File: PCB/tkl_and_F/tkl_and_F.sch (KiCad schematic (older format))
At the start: 18 parts

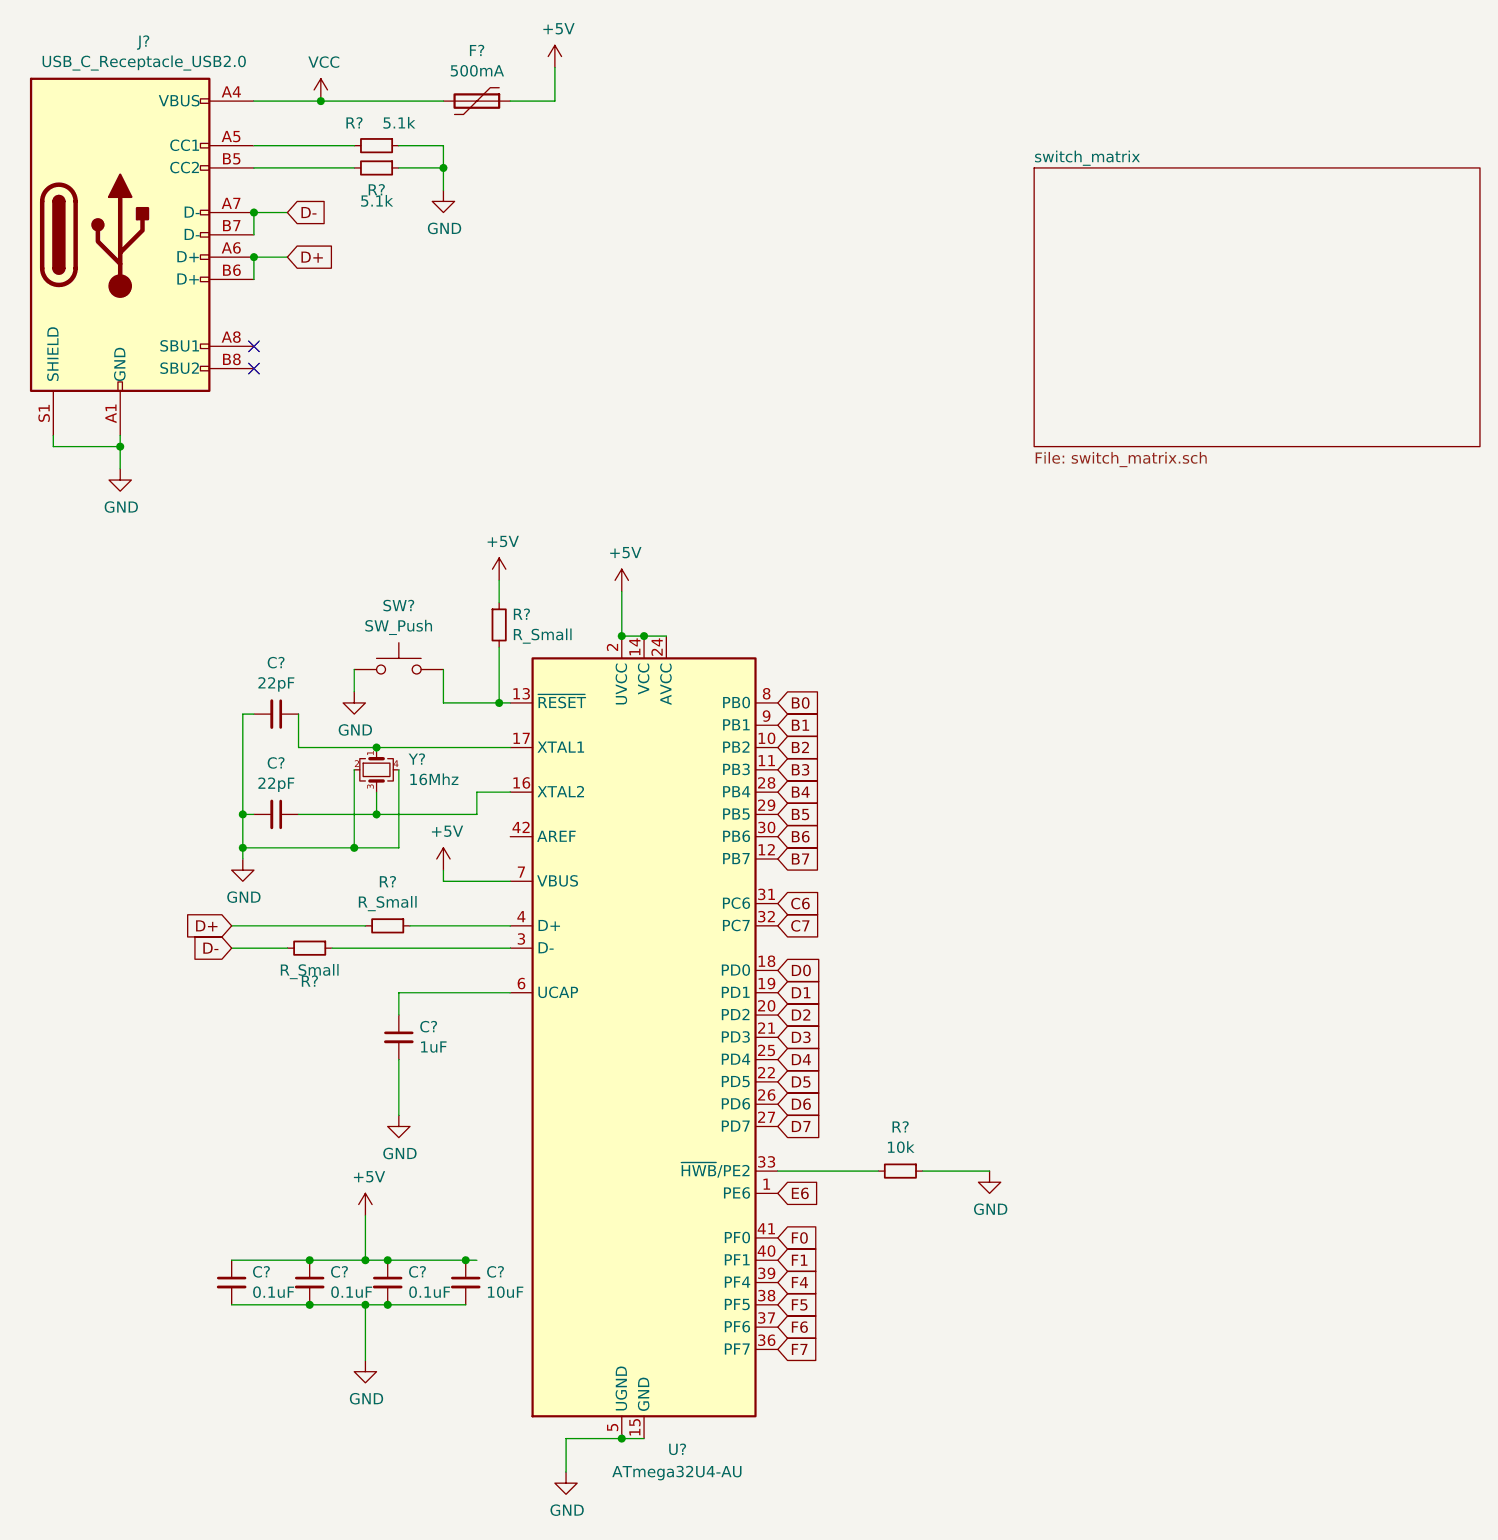
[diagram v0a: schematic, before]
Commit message: footprint assigment
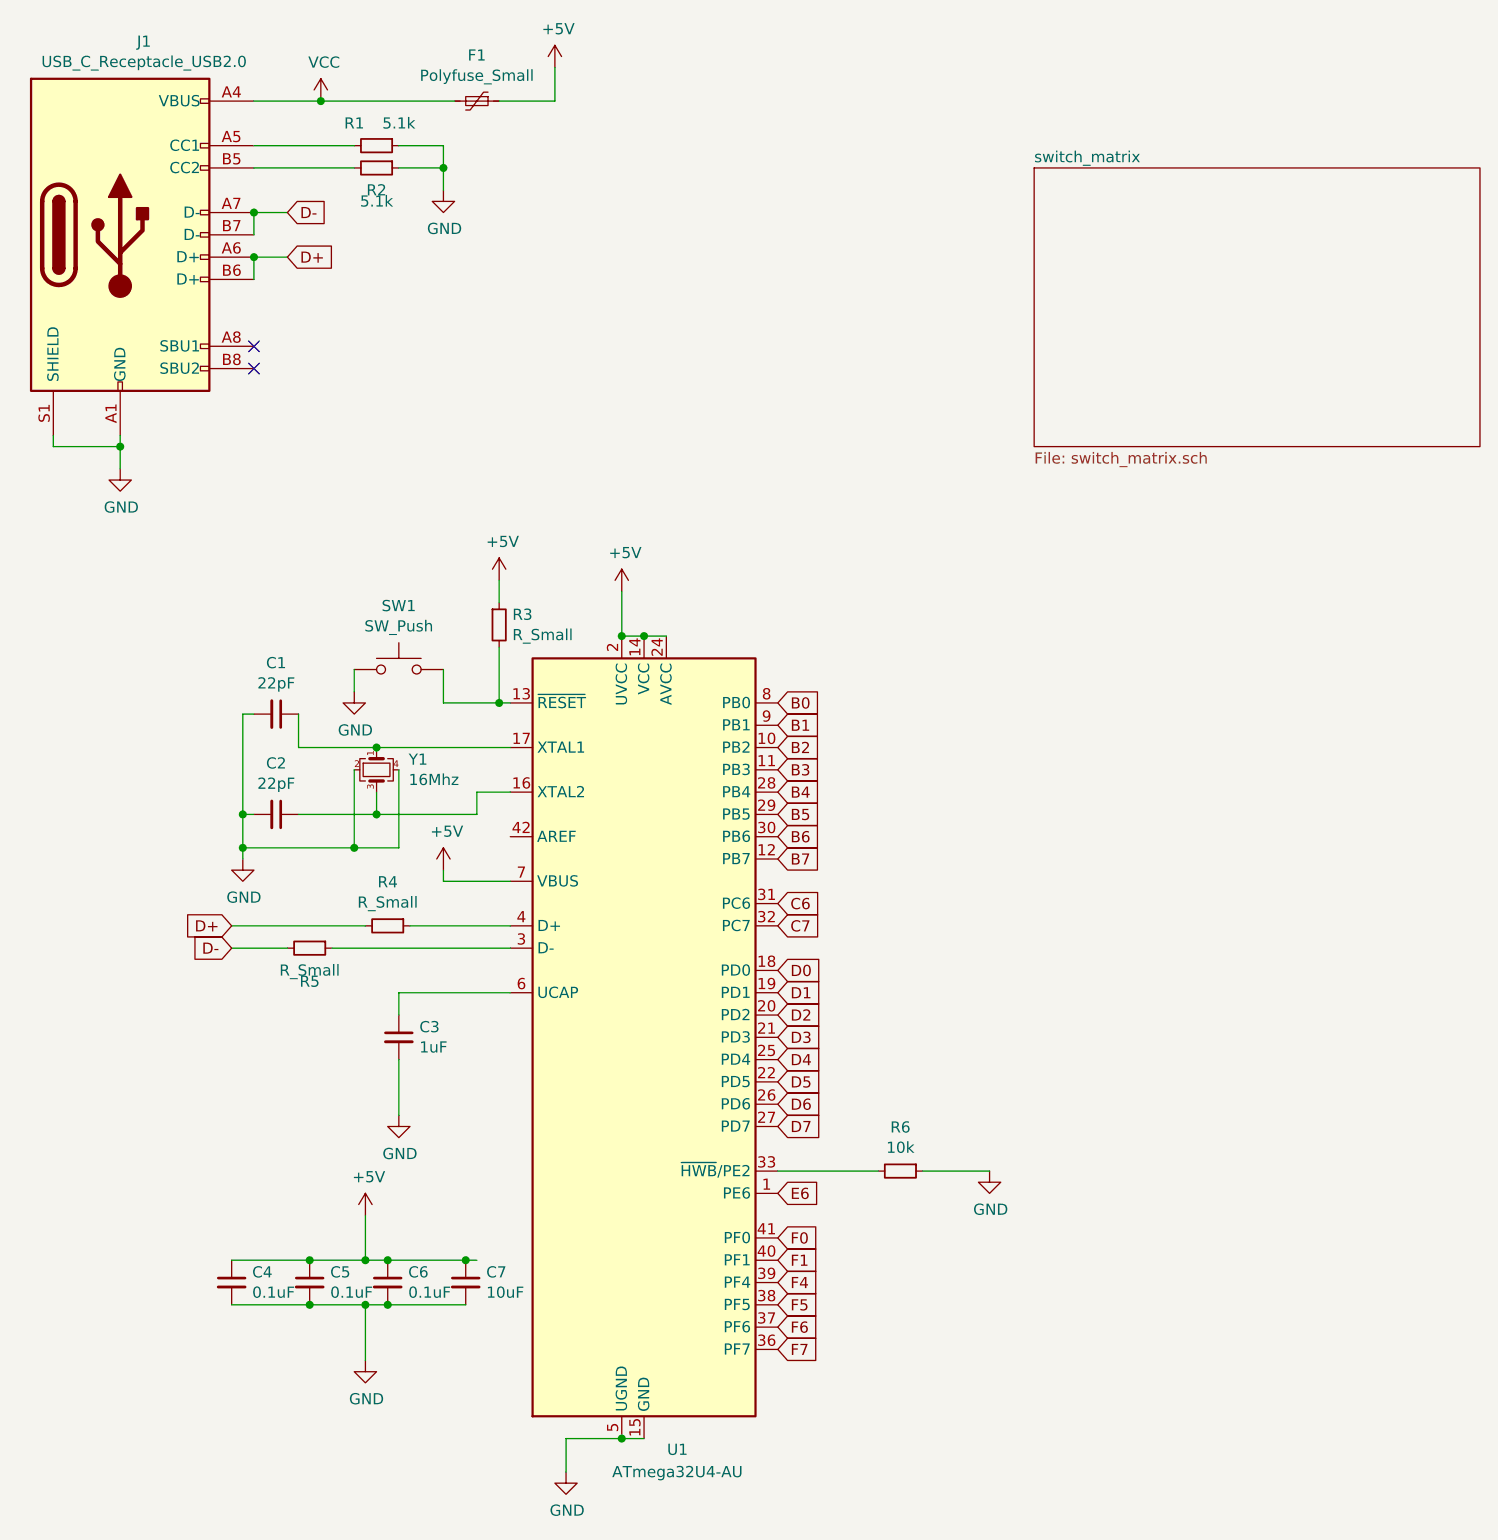
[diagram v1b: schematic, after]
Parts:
- removed F?: 500mA, symbol device:Polyfuse
- added F1: Polyfuse_Small, Fuse:Fuse_1206_3216Metric, symbol device:Polyfuse_Small
- C1, C2, C3, C4, C5, C6, C7: renamed from C?; footprint (none) -> Capacitors_SMD:C_0805
- J1: renamed from J?; footprint (none) -> Connectors_USB:USB_C_Receptacle_Amphenol_12401548E4-2A
- R1, R2, R3, R4, R5, R6: renamed from R?; footprint (none) -> Resistors_SMD:R_0805_HandSoldering
- SW1: renamed from SW?; footprint (none) -> random-keyboard-parts:SKQG-1155865
- Y1: renamed from Y?; footprint (none) -> Crystals:Crystal_SMD_3225-4pin_3.2x2.5mm_HandSoldering
- gave numbers to parts that had none: 1
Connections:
- net +5V: now also F1.1
- net VCC: now also F1.2
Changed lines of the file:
@@
 $EndDescr
 $Comp
-L MCU_Microchip_ATmega:ATmega32U4-AU U?
+L MCU_Microchip_ATmega:ATmega32U4-AU U1
 U 1 1 60163F7A
 P 3600 5300
-F 0 "U?" H 3750 3450 50  0000 C CNN
+F 0 "U1" H 3750 3450 50  0000 C CNN
 F 1 "ATmega32U4-AU" H 3750 3350 50  0000 C CNN
 F 2 "Package_QFP:TQFP-44_10x10mm_P0.8mm" H 3600 5300 50  0001 C CIN
@@
 	3250 7100 3250 7250
 $Comp
-L device:R_Small R?
+L device:R_Small R6
 U 1 1 6016CA00
 P 4750 5900
-F 0 "R?" V 4554 5900 50  0000 C CNN
+F 0 "R6" V 4554 5900 50  0000 C CNN
 F 1 "10k" V 4645 5900 50  0000 C CNN
-F 2 "" H 4750 5900 50  0001 C CNN
+F 2 "Resistors_SMD:R_0805_HandSoldering" H 4750 5900 50  0001 C CNN
 F 3 "~" H 4750 5900 50  0001 C CNN
 	1    4750 5900
@@
 	4850 5900 5150 5900
 $Comp
-L device:R_Small R?
+L device:R_Small R4
 U 1 1 6016D8AC
 P 2450 4800
-F 0 "R?" V 2254 4800 50  0000 C CNN
+F 0 "R4" V 2254 4800 50  0000 C CNN
 F 1 "R_Small" V 2345 4800 50  0000 C CNN
-F 2 "" H 2450 4800 50  0001 C CNN
+F 2 "Resistors_SMD:R_0805_HandSoldering" H 2450 4800 50  0001 C CNN
 F 3 "~" H 2450 4800 50  0001 C CNN
 	1    2450 4800
@@
 $EndComp
 $Comp
-L device:R_Small R?
+L device:R_Small R5
 U 1 1 6016DBEB
 P 2100 4900
-F 0 "R?" V 2250 4900 50  0000 C CNN
+F 0 "R5" V 2250 4900 50  0000 C CNN
 F 1 "R_Small" V 2200 4900 50  0000 C CNN
-F 2 "" H 2100 4900 50  0001 C CNN
+F 2 "Resistors_SMD:R_0805_HandSoldering" H 2100 4900 50  0001 C CNN
 F 3 "~" H 2100 4900 50  0001 C CNN
 	1    2100 4900
@@
 	1750 4800 2350 4800
 $Comp
-L device:C_Small C?
+L device:C_Small C3
 U 1 1 6016F54C
 P 2500 5300
-F 0 "C?" H 2592 5346 50  0000 L CNN
+F 0 "C3" H 2592 5346 50  0000 L CNN
 F 1 "1uF" H 2592 5255 50  0000 L CNN
-F 2 "" H 2500 5300 50  0001 C CNN
+F 2 "Capacitors_SMD:C_0805" H 2500 5300 50  0001 C CNN
 F 3 "~" H 2500 5300 50  0001 C CNN
 	1    2500 5300
@@
 	2500 5650 2500 5400
 $Comp
-L device:C_Small C?
+L device:C_Small C4
 U 1 1 60172033
 P 1750 6400
-F 0 "C?" H 1842 6446 50  0000 L CNN
+F 0 "C4" H 1842 6446 50  0000 L CNN
 F 1 "0.1uF" H 1842 6355 50  0000 L CNN
-F 2 "" H 1750 6400 50  0001 C CNN
+F 2 "Capacitors_SMD:C_0805" H 1750 6400 50  0001 C CNN
 F 3 "~" H 1750 6400 50  0001 C CNN
 	1    1750 6400
@@
 $EndComp
 $Comp
-L device:C_Small C?
+L device:C_Small C5
 U 1 1 60172E0F
 P 2100 6400
-F 0 "C?" H 2192 6446 50  0000 L CNN
+F 0 "C5" H 2192 6446 50  0000 L CNN
 F 1 "0.1uF" H 2192 6355 50  0000 L CNN
-F 2 "" H 2100 6400 50  0001 C CNN
+F 2 "Capacitors_SMD:C_0805" H 2100 6400 50  0001 C CNN
 F 3 "~" H 2100 6400 50  0001 C CNN
 	1    2100 6400
@@
 $EndComp
 $Comp
-L device:C_Small C?
+L device:C_Small C6
 U 1 1 6017313E
 P 2450 6400
-F 0 "C?" H 2542 6446 50  0000 L CNN
+F 0 "C6" H 2542 6446 50  0000 L CNN
 F 1 "0.1uF" H 2542 6355 50  0000 L CNN
-F 2 "" H 2450 6400 50  0001 C CNN
+F 2 "Capacitors_SMD:C_0805" H 2450 6400 50  0001 C CNN
 F 3 "~" H 2450 6400 50  0001 C CNN
 	1    2450 6400
@@
 $EndComp
 $Comp
-L device:C_Small C?
+L device:C_Small C7
 U 1 1 60173373
 P 2800 6400
-F 0 "C?" H 2892 6446 50  0000 L CNN
+F 0 "C7" H 2892 6446 50  0000 L CNN
 F 1 "10uF" H 2892 6355 50  0000 L CNN
-F 2 "" H 2800 6400 50  0001 C CNN
+F 2 "Capacitors_SMD:C_0805" H 2800 6400 50  0001 C CNN
 F 3 "~" H 2800 6400 50  0001 C CNN
 	1    2800 6400
@@
 $EndComp
 $Comp
-L device:Crystal_GND24_Small Y?
+L device:Crystal_GND24_Small Y1
 U 1 1 6017C43C
 P 2400 4100
-F 0 "Y?" V 2354 4244 50  0000 L CNN
+F 0 "Y1" V 2354 4244 50  0000 L CNN
 F 1 "16Mhz" V 2445 4244 50  0000 L CNN
-F 2 "" H 2400 4100 50  0001 C CNN
+F 2 "Crystals:Crystal_SMD_3225-4pin_3.2x2.5mm_HandSoldering" H 2400 4100 50  0001 C CNN
 F 3 "~" H 2400 4100 50  0001 C CNN
 	1    2400 4100
@@
 $EndComp
 $Comp
-L device:C_Small C?
+L device:C_Small C2
 U 1 1 6017FACA
 P 1950 4300
-F 0 "C?" V 1721 4300 50  0000 C CNN
+F 0 "C2" V 1721 4300 50  0000 C CNN
 F 1 "22pF" V 1812 4300 50  0000 C CNN
-F 2 "" H 1950 4300 50  0001 C CNN
+F 2 "Capacitors_SMD:C_0805" H 1950 4300 50  0001 C CNN
 F 3 "~" H 1950 4300 50  0001 C CNN
 	1    1950 4300
@@
 $EndComp
 $Comp
-L device:C_Small C?
+L device:C_Small C1
 U 1 1 60180A83
 P 1950 3850
-F 0 "C?" V 1721 3850 50  0000 C CNN
+F 0 "C1" V 1721 3850 50  0000 C CNN
 F 1 "22pF" V 1812 3850 50  0000 C CNN
-F 2 "" H 1950 3850 50  0001 C CNN
+F 2 "Capacitors_SMD:C_0805" H 1950 3850 50  0001 C CNN
 F 3 "~" H 1950 3850 50  0001 C CNN
 	1    1950 3850
@@
 Connection ~ 2400 4300
 $Comp
-L Switch:SW_Push SW?
+L Switch:SW_Push SW1
 U 1 1 6018A9D6
 P 2500 3650
-F 0 "SW?" H 2500 3935 50  0000 C CNN
+F 0 "SW1" H 2500 3935 50  0000 C CNN
 F 1 "SW_Push" H 2500 3844 50  0000 C CNN
-F 2 "" H 2500 3850 50  0001 C CNN
+F 2 "random-keyboard-parts:SKQG-1155865" H 2500 3850 50  0001 C CNN
 F 3 "~" H 2500 3850 50  0001 C CNN
 	1    2500 3650
@@
 $EndComp
 $Comp
-L device:R_Small R?
+L device:R_Small R3
 U 1 1 6018D8DA
 P 2950 3450
-F 0 "R?" H 3009 3496 50  0000 L CNN
+F 0 "R3" H 3009 3496 50  0000 L CNN
 F 1 "R_Small" H 3009 3405 50  0000 L CNN
-F 2 "" H 2950 3450 50  0001 C CNN
+F 2 "Resistors_SMD:R_0805_HandSoldering" H 2950 3450 50  0001 C CNN
 F 3 "~" H 2950 3450 50  0001 C CNN
 	1    2950 3450
@@
 	1250 2650 1250 2600
 $Comp
-L Connector:USB_C_Receptacle_USB2.0 J?
+L Connector:USB_C_Receptacle_USB2.0 J1
 U 1 1 601B9FC4
 P 1250 1700
-F 0 "J?" H 1357 2567 50  0000 C CNN
+F 0 "J1" H 1357 2567 50  0000 C CNN
 F 1 "USB_C_Receptacle_USB2.0" H 1357 2476 50  0000 C CNN
-F 2 "" H 1400 1700 50  0001 C CNN
+F 2 "Connectors_USB:USB_C_Receptacle_Amphenol_12401548E4-2A" H 1400 1700 50  0001 C CNN
 F 3 "https://www.usb.org/sites/default/files/documents/usb_type-c.zip" H 1400 1700 50  0001 C CNN
 	1    1250 1700
@@
 NoConn ~ 1850 2300
 $Comp
-L device:R_Small R?
+L device:R_Small R2
 U 1 1 601C0F74
 P 2400 1400
-F 0 "R?" V 2500 1400 50  0000 C CNN
+F 0 "R2" V 2500 1400 50  0000 C CNN
 F 1 "5.1k" V 2550 1400 50  0000 C CNN
-F 2 "" H 2400 1400 50  0001 C CNN
+F 2 "Resistors_SMD:R_0805_HandSoldering" H 2400 1400 50  0001 C CNN
 F 3 "~" H 2400 1400 50  0001 C CNN
 	1    2400 1400
@@
 $EndComp
 $Comp
-L device:R_Small R?
+L device:R_Small R1
 U 1 1 601C222D
 P 2400 1300
-F 0 "R?" V 2300 1200 50  0000 C CNN
+F 0 "R1" V 2300 1200 50  0000 C CNN
 F 1 "5.1k" V 2300 1400 50  0000 C CNN
-F 2 "" H 2400 1300 50  0001 C CNN
+F 2 "Resistors_SMD:R_0805_HandSoldering" H 2400 1300 50  0001 C CNN
 F 3 "~" H 2400 1300 50  0001 C CNN
 	1    2400 1300
@@
 Wire Wire Line
 	1850 1400 2300 1400
-$Comp
-L device:Polyfuse F?
-U 1 1 601D1243
-P 2850 1100
-F 0 "F?" V 2625 1100 50  0000 C CNN
-F 1 "500mA" V 2716 1100 50  0000 C CNN
-F 2 "" H 2900 900 50  0001 L CNN
-F 3 "~" H 2850 1100 50  0001 C CNN
-	1    2850 1100
-	0    1    1    0
-$EndComp
 Wire Wire Line
 	3200 950  3200 1100
-Wire Wire Line
-	3200 1100 3000 1100
 Wire Wire Line
 	1850 1100 2150 1100
@@
 $EndComp
 Connection ~ 2150 1100
-Wire Wire Line
-	2150 1100 2700 1100
 $Sheet
 S 5350 1400 2000 1250
@@
 Text GLabel 4200 6700 2    50   Input ~ 0
 F7
+$Comp
+L device:Polyfuse_Small F1
+U 1 1 611B3EDB
+P 2850 1100
+F 0 "F1" V 2645 1100 50  0000 C CNN
+F 1 "Polyfuse_Small" V 2736 1100 50  0000 C CNN
+F 2 "Fuse:Fuse_1206_3216Metric" H 2900 900 50  0001 L CNN
+F 3 "~" H 2850 1100 50  0001 C CNN
+	1    2850 1100
+	0    1    1    0
+$EndComp
+Wire Wire Line
+	2150 1100 2750 1100
+Wire Wire Line
+	2950 1100 3200 1100
 $EndSCHEMATC
